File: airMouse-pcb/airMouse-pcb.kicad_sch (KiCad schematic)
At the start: 11 parts, among them Q1 IRLML6346, U1 STM32G071RBTx, U2 AP1603

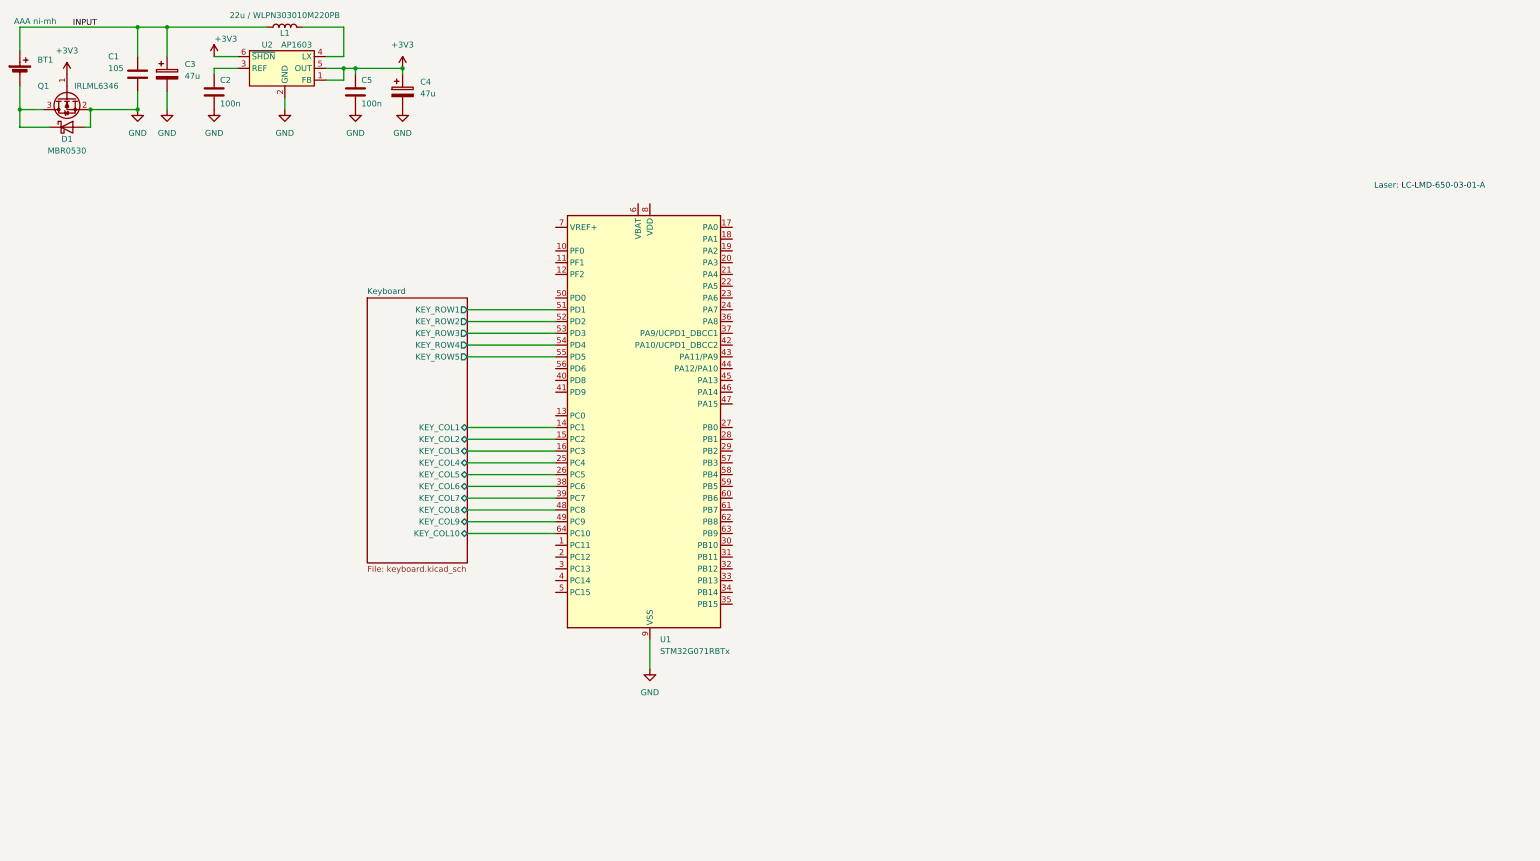
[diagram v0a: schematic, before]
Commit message: add keyboard
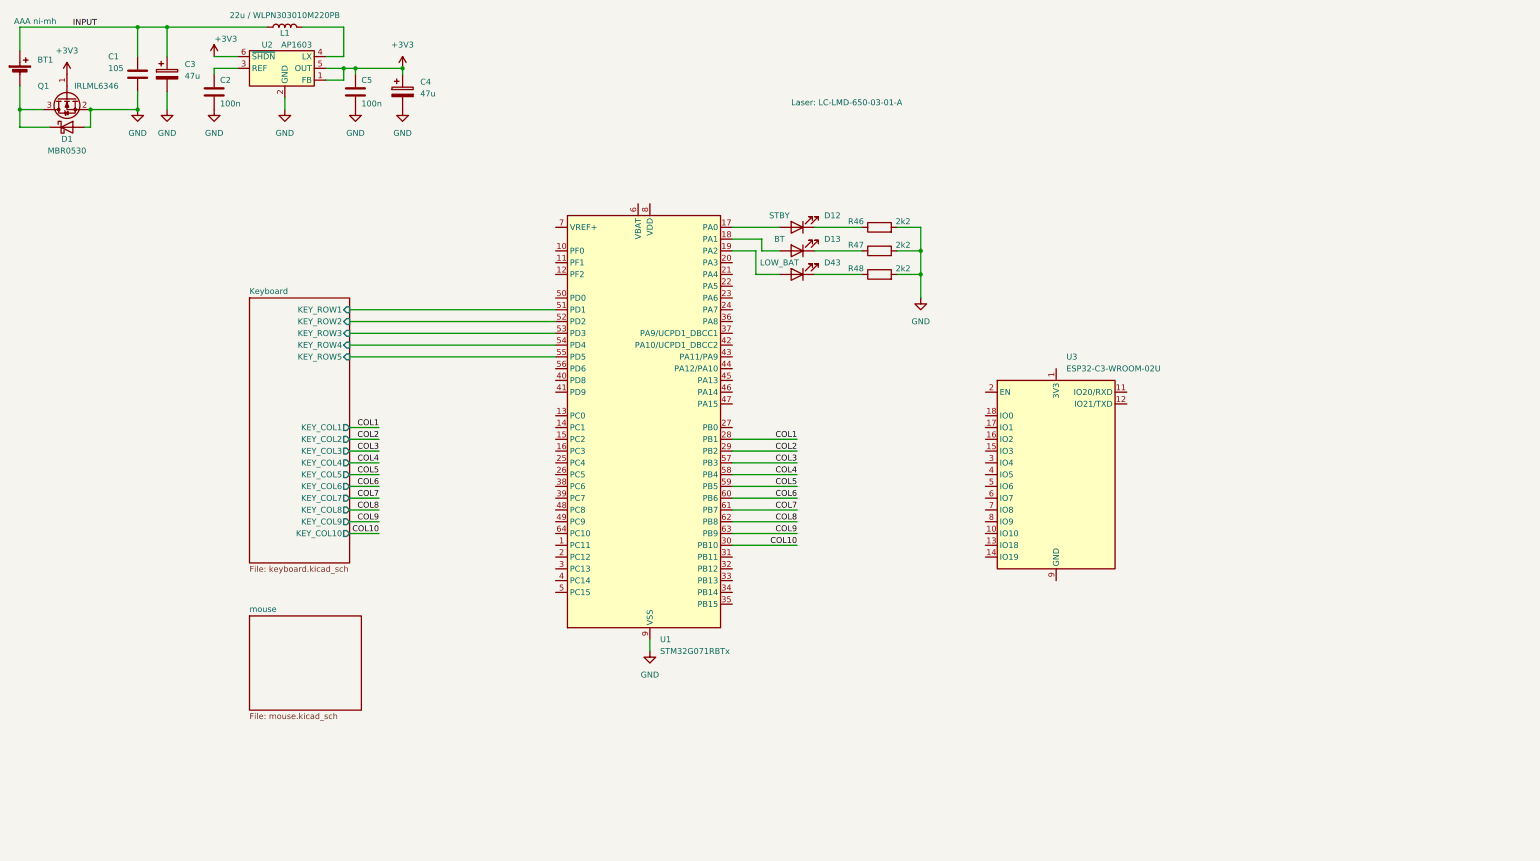
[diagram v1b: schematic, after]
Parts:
- added D12: STBY, symbol Device:LED
- added D13: BT, symbol Device:LED
- added D43: LOW_BAT, symbol Device:LED
- added R46, R47, R48: 2k2, symbol Device:R
- added U3: ESP32-C3-WROOM-02U, RF_Module:ESP32-C3-WROOM-02U, symbol RF_Module:ESP32-C3-WROOM-02U
- C1, C2, C3, C5: footprint (none) -> Capacitor_SMD:C_0603_1608Metric
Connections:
- net GND: now also R46.2, R47.2, R48.2
- net at U1.17 (PA0): now also D12.2 (A)
- net at U1.18 (PA1): now also D13.2 (A)
- net at U1.19 (PA2): now also D43.2 (A)
- net COL1: now reaches U1.28 (PB1)
- net COL2: now reaches U1.29 (PB2)
- net COL10: now reaches U1.30 (PB10)
- net COL3: now reaches U1.57 (PB3)
- net COL4: now reaches U1.58 (PB4)
- net COL5: now reaches U1.59 (PB5)
- net COL6: now reaches U1.60 (PB6)
- net COL7: now reaches U1.61 (PB7)
- net COL8: now reaches U1.62 (PB8)
- net COL9: now reaches U1.63 (PB9)
- net Keyboard/KEY_COL1: no longer names the net of U1.14 (PC1)
- net Keyboard/KEY_COL10: no longer names the net of U1.64 (PC10)
- net Keyboard/KEY_COL2: no longer names the net of U1.15 (PC2)
- net Keyboard/KEY_COL3: no longer names the net of U1.16 (PC3)
- net Keyboard/KEY_COL4: no longer names the net of U1.25 (PC4)
- net Keyboard/KEY_COL5: no longer names the net of U1.26 (PC5)
- net Keyboard/KEY_COL6: no longer names the net of U1.38 (PC6)
- net Keyboard/KEY_COL7: no longer names the net of U1.39 (PC7)
- net Keyboard/KEY_COL8: no longer names the net of U1.48 (PC8)
- net Keyboard/KEY_COL9: no longer names the net of U1.49 (PC9)
- new net: D12.1 (K), R46.1
- new net: D43.1 (K), R48.1
- new net: U3.19 (GND), U3.9 (GND)
- new net: D13.1 (K), R47.1
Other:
- added sheet mouse (mouse.kicad_sch)

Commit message: schematic
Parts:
- added C26, C29, C31, C33, C34: 100n, Capacitor_SMD:C_0603_1608Metric, symbol Device:C
- added C27: 4u7, Capacitor_SMD:C_0805_2012Metric, symbol Device:C
- added C28, C30: 1u, Capacitor_SMD:C_0603_1608Metric, symbol Device:C
- added C32: 10u, Capacitor_SMD:C_0805_2012Metric, symbol Device:C
- added FB1: 600R @ 100M, Capacitor_SMD:C_0603_1608Metric, symbol Device:FerriteBead
- added J4: AT, Connector_JST:JST_ZH_S3B-ZR-SM4A-TF_1x03-1MP_P1.50mm_Horizontal, symbol airMouseLib:Conn_01x03_MP
- added J5: RADIO_PRG, Connector_JST:JST_ZH_S3B-ZR-SM4A-TF_1x03-1MP_P1.50mm_Horizontal, symbol airMouseLib:Conn_01x03_MP
- added J6: MCU_PRG, Connector_JST:JST_ZH_S5B-ZR-SM4A-TF_1x05-1MP_P1.50mm_Horizontal, symbol airMouseLib:Conn_01x05_MP
- added LD1: 70115420, Connector_PinHeader_2.54mm:PinHeader_1x02_P2.54mm_Vertical, symbol Device:D_Laser_1C2A
- added R49, R50, R53, R54, R55, R56, R58, R59: 10k, Resistor_SMD:R_0603_1608Metric, symbol Device:R
- added R51, R52: 4k7, Resistor_SMD:R_0603_1608Metric, symbol Device:R
- added R57: 2k2, Resistor_SMD:R_0603_1608Metric, symbol Device:R
- added R60, R61: 0R, Resistor_SMD:R_0603_1608Metric, symbol Device:R
- added SW60: KEY, airMouseLib:TL3315NF100Q, symbol airMouseLib:KEY
- added TP1: DBG_TX, TestPoint:TestPoint_Pad_D1.0mm, symbol Connector:TestPoint
- added TP2: DBG_RX, TestPoint:TestPoint_Pad_D1.0mm, symbol Connector:TestPoint
- added U4: LSM6DS3, Package_LGA:LGA-14_3x2.5mm_P0.5mm_LayoutBorder3x4y, symbol Sensor_Motion:LSM6DS3
- BT1: value AAA ni-mh -> BC-0401; footprint (none) -> airMouseLib:BC-0401; Field5 (none) -> AAA Ni-MH
- C3: footprint Capacitor_SMD:C_0603_1608Metric -> Capacitor_SMD:CP_Elec_6.3x5.8; Field5 (none) -> EEHZC1V470P
- C4: footprint (none) -> Capacitor_SMD:CP_Elec_6.3x5.8; Field5 (none) -> EEHZC1V470P
- D12, D13, D43: footprint (none) -> LED_SMD:LED_0603_1608Metric
- R46, R47, R48: footprint (none) -> Resistor_SMD:R_0603_1608Metric
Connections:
- net +3V3: now also U1.6 (VBAT), U1.8 (VDD), U3.1 (3V3), C26.1, C27.1, C28.1, C31.1, C32.1, C33.1, C34.1, FB1.1, J6.1 (Pin_1), R49.1, R51.1, R52.1, R53.1, R54.1, R55.1, R56.1, R58.1, SW60.2 (B), U4.5 (VDDIO), U4.8 (VDD)
- net GND: now also U3.19 (GND), U3.9 (GND), C26.2, C27.2, C28.2, C29.2, C30.2, C31.2, C32.2, C33.2, C34.2, J4.3 (Pin_3), J4.MP (Pin_3), J5.3 (Pin_3), J5.MP (Pin_3), J6.3 (Pin_3), J6.MP (Pin_5), LD1.1 (K), R50.2, R59.2, R60.2, R61.2, U4.6 (GND), U4.7 (GND)
- net BAT-: now reaches BT1.2 (-), D1.1 (K), Q1.3 (D)
- net at D12.2 (A): now also U1.22 (PA5); no longer U1.17 (PA0)
- net at D43.2 (A): now also U1.21 (PA4); no longer U1.19 (PA2)
- net PRG_ESP_RX: now reaches U3.11 (IO20/RXD)
- net PRG_ESP_RX: now also J5.1 (Pin_1)
- net PRG_ESP_TX: now reaches U3.12 (IO21/TXD)
- net PRG_ESP_TX: now also J5.2 (Pin_2)
- net at U3.16 (IO2): now also R56.2
- net ESP_RST: now reaches U3.2 (EN)
- net ESP_RST: now also U1.35 (PB15), C30.1, R54.2
- net AT_MCU_TX: now reaches U3.5 (IO6)
- net AT_MCU_TX: now also U1.25 (PC4), J4.1 (Pin_1)
- net AT_MCU_RX: now reaches U3.6 (IO7)
- net AT_MCU_RX: now also U1.26 (PC5), J4.2 (Pin_2)
- net at U3.7 (IO8): now also R53.2
- net ESP_BOOT: now reaches U3.8 (IO9)
- net ESP_BOOT: now also U1.34 (PB14), R55.2
- net mouse/MOUSE_FWD: now reaches U1.1 (PC11)
- net RST: now reaches U1.12 (PF2)
- net RST: now also J6.5 (Pin_5), R49.2
- net mouse/MOUSE_BACK: now reaches U1.2 (PC12)
- net DBR_RX: now reaches U1.20 (PA3)
- net DBR_RX: now also TP2.1
- net mouse/MOUSE_DPI: now reaches U1.3 (PC13)
- net SCL: now reaches U1.37 (PA9/UCPD1_DBCC1)
- net SCL: now also R52.2, U4.13 (SCL)
- net mouse/MOUSE_LB: now reaches U1.38 (PC6)
- net mouse/MOUSE_MB: now reaches U1.39 (PC7)
- net mouse/MOUSE_PRC: now reaches U1.4 (PC14)
- net SDA: now reaches U1.42 (PA10/UCPD1_DBCC2)
- net SDA: now also R51.2, U4.14 (SDA)
- net SWDIO: now reaches U1.45 (PA13)
- net SWDIO: now also J6.4 (Pin_4)
- net SWDCLK: now reaches U1.46 (PA14)
- net SWDCLK: now also J6.2 (Pin_2), R50.1
- net mouse/MOUSE_RB: now reaches U1.48 (PC8)
- net mouse/MOUSE_UP: now reaches U1.49 (PC9)
- net mouse/MOUSE_HOME: now reaches U1.5 (PC15)
- net mouse/MOUSE_DN: now reaches U1.64 (PC10)
- net at U1.7 (VREF+): now also C29.1, FB1.2
- net INPUT renamed BAT+
- new net: LD1.2 (A), R57.1
- new net: R57.2, SW60.1 (A)
- new net: R58.2, U4.12 (CS)
- new net: R59.1, U4.1 (SDO/SA0)
- new net DBG_TX: TP1.1, U1.19 (PA2)
- new net GYRO_INT: U1.17 (PA0), U4.4 (INT1)
- new net SCX: R60.1, U4.3 (SCX)
- new net SDX: R61.1, U4.2 (SDX)
- no-connect marks 0 -> 29
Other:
- sheet mouse ports: added MOUSE_BACK, MOUSE_DN, MOUSE_DPI, MOUSE_FWD, MOUSE_HOME, MOUSE_LB, MOUSE_MB, MOUSE_PRC, MOUSE_RB, MOUSE_UP; removed none
- note added: "additional parts: 1x ZH plug ZHR-3 1x ZH plug ZHR-5 8x ZH pin w/ cable SZH-200BK26"
- note removed: "Laser: LC-LMD-650-03-01-A"
- moved on the sheet: BT1, C1, C2, C3, C4, C5, D1, D13, D43, L1, Q1, R47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

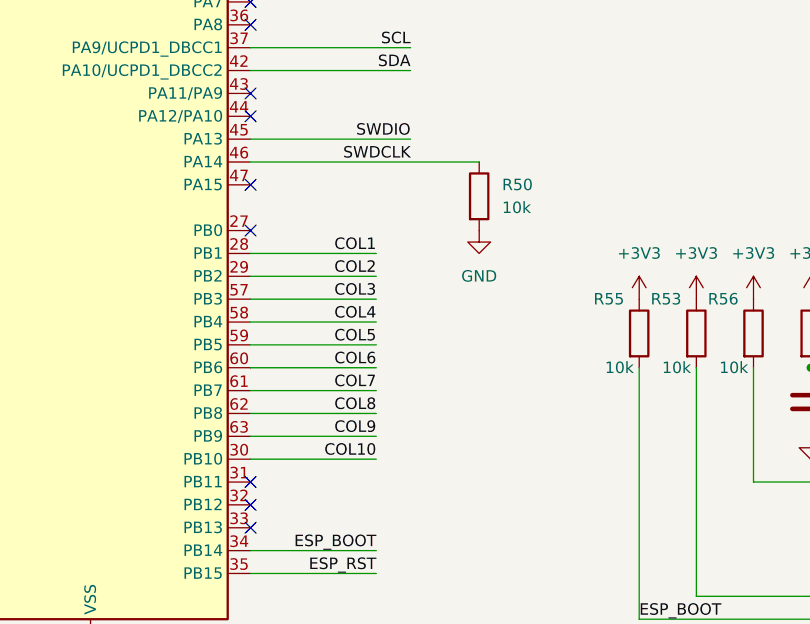
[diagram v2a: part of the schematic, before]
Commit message: add adc channel
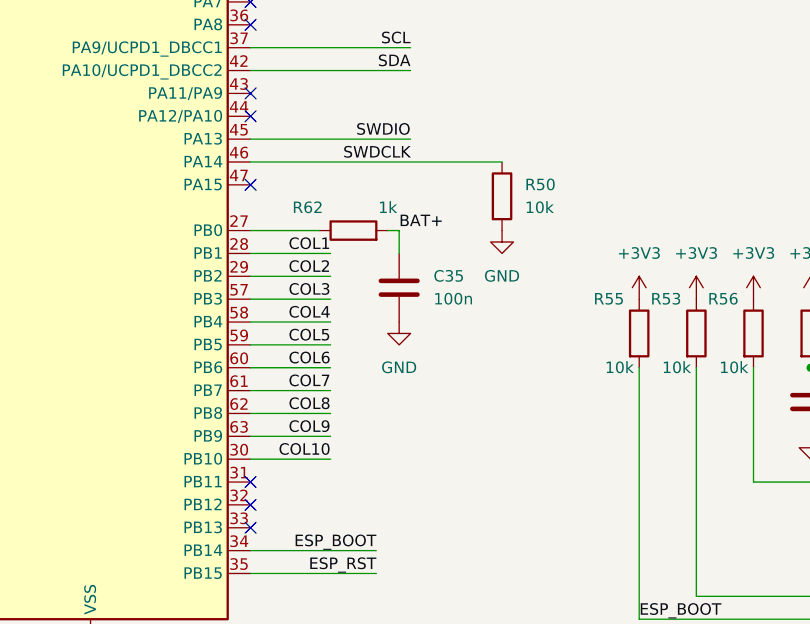
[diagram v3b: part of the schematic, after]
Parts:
- added C35: 100n, Capacitor_SMD:C_0603_1608Metric, symbol Device:C
- added R62: 1k, symbol Device:R
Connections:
- net BAT+: now also C35.1, R62.2
- net GND: now also C35.2
- net at U1.27 (PB0): now also R62.1
- no-connect marks 29 -> 28
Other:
- moved on the sheet: R50

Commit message: page data
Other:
- company: (none) -> Bart's Design
- title: (none) -> EtherPointer
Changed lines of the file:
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@@
 	(generator_version "8.0")
 	(paper "A4")
+	(title_block
+		(title "EtherPointer")
+		(date "2025-02-13")
+		(rev "RC1")
+		(company "Bart's Design")
+		(comment 1 "Bartosz Pracz")
+	)
 	(junction
 		(at 62.23 148.59)
@@
 	(text "additional parts:\n1x ZH plug ZHR-3\n1x ZH plug ZHR-5\n8x ZH pin w/ cable SZH-200BK26"
 		(exclude_from_sim no)
-		(at 184.15 172.72 0)
+		(at 179.07 171.45 0)
 		(effects
 			(font
